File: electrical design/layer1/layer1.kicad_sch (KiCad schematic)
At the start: 225 parts, among them J1 XT30-F, J10 Conn_01x02_Pin, J11 Conn_01x01_Socket, J12 Conn_01x01_Socket, J13 Conn_01x05_Pin, J14 Conn_01x02_Pin, J2 Conn_01x01_Socket, J3 Conn_01x01_Socket, J4 XT30PW-F, J5 Conn_01x01_Socket, J6 Conn_01x01_Socket, J7 Conn_01x01_Socket, J8 Conn_01x01_Socket, J9 Conn_01x02_Pin, Q1 MOSFET-NCH-FQP30N06L, Q2 MOSFET-NCH-AO3404A, SW1 SW_SPDT, U1 CD74HC4067SM, U2 CD74HC4067SM, U3 MOUDLE-SEEEDUINO-XIAO-ESP32C3

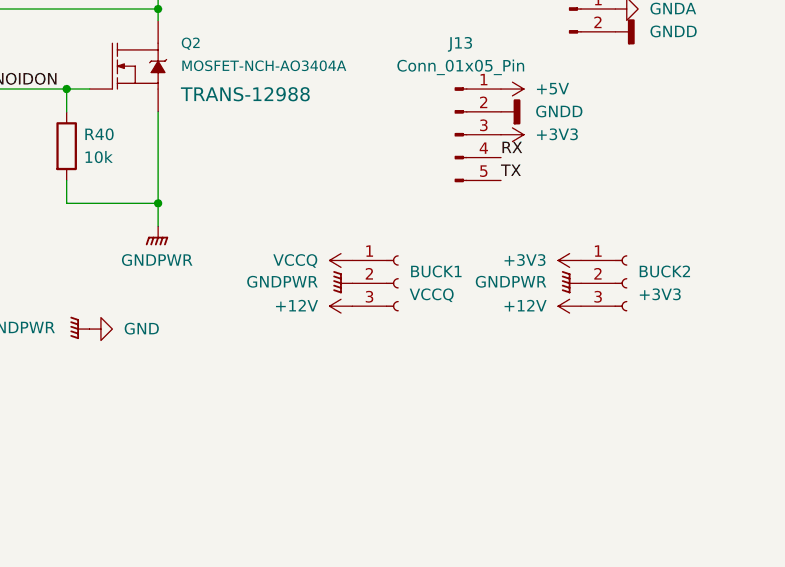
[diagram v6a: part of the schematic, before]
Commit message: amend buck conv pinouts on l1 and l3
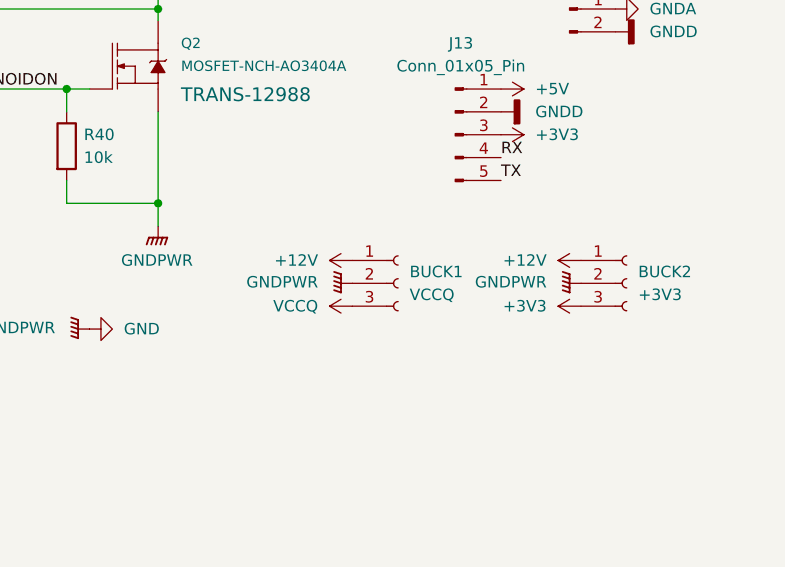
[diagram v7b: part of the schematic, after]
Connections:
- net +12V: now also BUCK1.1 (Pin_1), BUCK2.1 (Pin_1); no longer BUCK1.3 (Pin_3), BUCK2.3 (Pin_3)
- net +3V3: now also BUCK2.3 (Pin_3); no longer BUCK2.1 (Pin_1)
- net VCCQ: now also BUCK1.3 (Pin_3); no longer BUCK1.1 (Pin_1)
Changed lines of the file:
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@@
     )
   )
+  (symbol (lib_name "VCCQ_2") (lib_id "power:VCCQ") (at 245.11 156.21 90) (unit 1)
+    (in_bom yes) (on_board yes) (dnp no) (fields_autoplaced)
+    (property "Reference" "#PWR019" (at 248.92 156.21 0)
+      (effects (font (size 1.27 1.27)) hide)
+    )
+    (property "Value" "VCCQ" (at 241.3 156.21 90)
+      (effects (font (size 1.27 1.27)) (justify left))
+    )
+    (property "Footprint" "" (at 245.11 156.21 0)
+      (effects (font (size 1.27 1.27)) hide)
+    )
+    (property "Datasheet" "" (at 245.11 156.21 0)
+      (effects (font (size 1.27 1.27)) hide)
+    )
+    (pin "1")
+    (instances
+      (project "layer1"
+        (path "/32d54464-fd6f-441d-9cef-d3e4fabf9fe1"
+          (reference "#PWR019") (unit 1)
+        )
+      )
+    )
+  )
   (symbol (lib_id "Connector:Conn_01x02_Pin") (at 269.24 123.19 0) (unit 1)
     (in_bom yes) (on_board yes) (dnp no) (fields_autoplaced)
@@
     )
   )
-  (symbol (lib_name "+12V_2") (lib_id "power:+12V") (at 270.51 156.21 90) (unit 1)
+  (symbol (lib_name "+12V_2") (lib_id "power:+12V") (at 270.51 151.13 90) (unit 1)
     (in_bom yes) (on_board yes) (dnp no) (fields_autoplaced)
-    (property "Reference" "#PWR024" (at 274.32 156.21 0)
+    (property "Reference" "#PWR024" (at 274.32 151.13 0)
       (effects (font (size 1.27 1.27)) hide)
     )
-    (property "Value" "+12V" (at 266.7 156.21 90)
+    (property "Value" "+12V" (at 266.7 151.13 90)
       (effects (font (size 1.27 1.27)) (justify left))
     )
-    (property "Footprint" "" (at 270.51 156.21 0)
+    (property "Footprint" "" (at 270.51 151.13 0)
       (effects (font (size 1.27 1.27)) hide)
     )
-    (property "Datasheet" "" (at 270.51 156.21 0)
+    (property "Datasheet" "" (at 270.51 151.13 0)
       (effects (font (size 1.27 1.27)) hide)
     )
@@
     )
   )
+  (symbol (lib_id "power:+3V3") (at 270.51 156.21 90) (unit 1)
+    (in_bom yes) (on_board yes) (dnp no) (fields_autoplaced)
+    (property "Reference" "#PWR021" (at 274.32 156.21 0)
+      (effects (font (size 1.27 1.27)) hide)
+    )
+    (property "Value" "+3V3" (at 266.7 156.2101 90)
+      (effects (font (size 1.27 1.27)) (justify left))
+    )
+    (property "Footprint" "" (at 270.51 156.21 0)
+      (effects (font (size 1.27 1.27)) hide)
+    )
+    (property "Datasheet" "" (at 270.51 156.21 0)
+      (effects (font (size 1.27 1.27)) hide)
+    )
+    (pin "1")
+    (instances
+      (project "layer1"
+        (path "/32d54464-fd6f-441d-9cef-d3e4fabf9fe1"
+          (reference "#PWR021") (unit 1)
+        )
+      )
+      (project "layer3"
+        (path "/d3bc7e0f-ae6c-4cdf-9591-eb9484f67211"
+          (reference "#PWR0111") (unit 1)
+        )
+      )
+    )
+  )
   (symbol (lib_id "pspice:INDUCTOR") (at 212.09 59.69 90) (unit 1)
     (in_bom yes) (on_board yes) (dnp no) (fields_autoplaced)
@@
     )
   )
-  (symbol (lib_name "VCCQ_2") (lib_id "power:VCCQ") (at 245.11 151.13 90) (unit 1)
-    (in_bom yes) (on_board yes) (dnp no) (fields_autoplaced)
-    (property "Reference" "#PWR019" (at 248.92 151.13 0)
-      (effects (font (size 1.27 1.27)) hide)
-    )
-    (property "Value" "VCCQ" (at 241.3 151.13 90)
-      (effects (font (size 1.27 1.27)) (justify left))
-    )
-    (property "Footprint" "" (at 245.11 151.13 0)
-      (effects (font (size 1.27 1.27)) hide)
-    )
-    (property "Datasheet" "" (at 245.11 151.13 0)
-      (effects (font (size 1.27 1.27)) hide)
-    )
-    (pin "1")
-    (instances
-      (project "layer1"
-        (path "/32d54464-fd6f-441d-9cef-d3e4fabf9fe1"
-          (reference "#PWR019") (unit 1)
-        )
-      )
-    )
-  )
   (symbol (lib_id "Device:FerriteBead") (at 187.325 155.575 90) (unit 1)
     (in_bom yes) (on_board yes) (dnp no) (fields_autoplaced)
@@
     )
   )
-  (symbol (lib_id "power:+3V3") (at 270.51 151.13 90) (unit 1)
-    (in_bom yes) (on_board yes) (dnp no) (fields_autoplaced)
-    (property "Reference" "#PWR021" (at 274.32 151.13 0)
-      (effects (font (size 1.27 1.27)) hide)
-    )
-    (property "Value" "+3V3" (at 266.7 151.1301 90)
-      (effects (font (size 1.27 1.27)) (justify left))
-    )
-    (property "Footprint" "" (at 270.51 151.13 0)
-      (effects (font (size 1.27 1.27)) hide)
-    )
-    (property "Datasheet" "" (at 270.51 151.13 0)
-      (effects (font (size 1.27 1.27)) hide)
-    )
-    (pin "1")
-    (instances
-      (project "layer1"
-        (path "/32d54464-fd6f-441d-9cef-d3e4fabf9fe1"
-          (reference "#PWR021") (unit 1)
-        )
-      )
-      (project "layer3"
-        (path "/d3bc7e0f-ae6c-4cdf-9591-eb9484f67211"
-          (reference "#PWR0111") (unit 1)
-        )
-      )
-    )
-  )
   (symbol (lib_id "power:GNDPWR") (at 181.61 142.24 90) (unit 1)
     (in_bom yes) (on_board yes) (dnp no) (fields_autoplaced)
@@
     )
   )
-  (symbol (lib_name "+12V_2") (lib_id "power:+12V") (at 245.11 156.21 90) (unit 1)
+  (symbol (lib_name "+12V_2") (lib_id "power:+12V") (at 245.11 151.13 90) (unit 1)
     (in_bom yes) (on_board yes) (dnp no) (fields_autoplaced)
-    (property "Reference" "#PWR023" (at 248.92 156.21 0)
+    (property "Reference" "#PWR023" (at 248.92 151.13 0)
       (effects (font (size 1.27 1.27)) hide)
     )
-    (property "Value" "+12V" (at 241.3 156.21 90)
+    (property "Value" "+12V" (at 241.3 151.13 90)
       (effects (font (size 1.27 1.27)) (justify left))
     )
-    (property "Footprint" "" (at 245.11 156.21 0)
+    (property "Footprint" "" (at 245.11 151.13 0)
       (effects (font (size 1.27 1.27)) hide)
     )
-    (property "Datasheet" "" (at 245.11 156.21 0)
+    (property "Datasheet" "" (at 245.11 151.13 0)
       (effects (font (size 1.27 1.27)) hide)
     )

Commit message: finalise pcbs for production
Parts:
- removed J14: Conn_01x02_Pin, Connector_JST:JST_SH_BM02B-SRSS-TB_1x02-1MP_P1.00mm_Vertical, symbol Connector:Conn_01x02_Pin
- added J14: SH1.0 3P, Connector_JST:JST_SH_BM03B-SRSS-TB_1x03-1MP_P1.00mm_Vertical, symbol Connector:Conn_01x03_Pin
- added J15: Conn_01x01_Socket, Connector_Wire:SolderWirePad_1x01_SMD_1x2mm, symbol Connector:Conn_01x01_Socket
- J13: value Conn_01x05_Pin -> SH1.0 5P
- R1, R10, R11, R12, R13, R14, R15, R16, R17, R18, R19, R2, R20, R21, R22, R23, R24, R25, R26, R27, R28, R29, R3, R30, R31, R32, R4, R5, R6, R7, R8, R9: value 0.39 -> 0R39
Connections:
- net +3V3: now also J14.3 (Pin_3)
- net GND: now also J15.1 (Pin_1)
- net GNDA: now also J14.1 (Pin_1)
- net GNDD: now also J14.2 (Pin_2)
